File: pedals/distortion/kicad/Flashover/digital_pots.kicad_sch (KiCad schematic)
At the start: 5 parts, among them U7 MCP45HV51-104, U8 MCP45HV51-103, U9 MCP45HV51-103

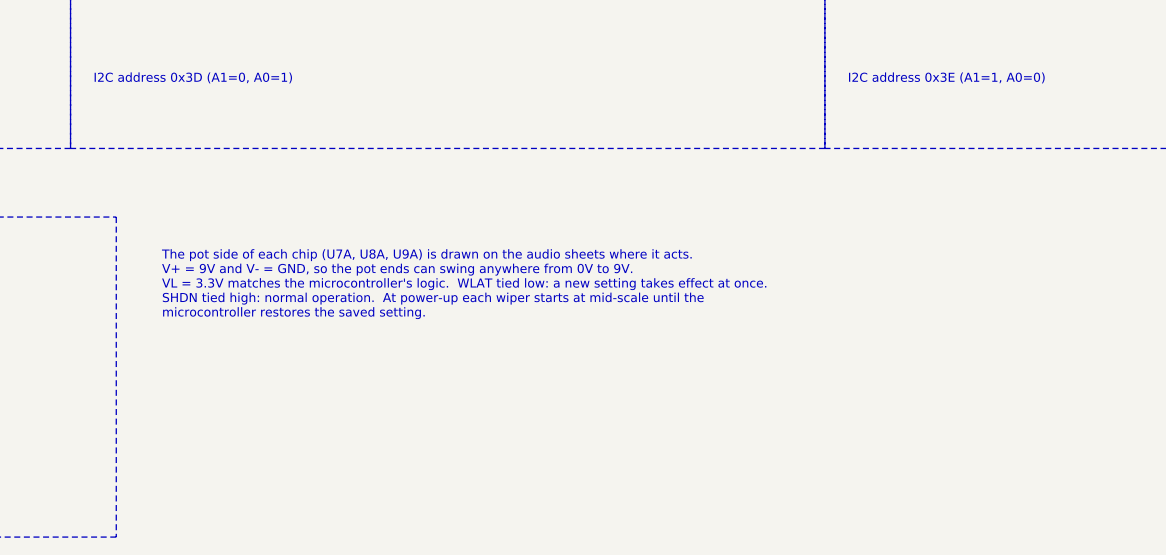
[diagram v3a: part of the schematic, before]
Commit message: Apply datasheet checks to Flashover
R33 = 15k (about 5 mA per LED, from the IS31FL3236A current formula).
R39 marked 33 ohm 0.5W per MIDI CA-033. R4 390 -> 330 because the
MCP45HV51 wiper resistance is about 150 ohms at 9V (below its 10V
specified range); sim model Rw updated to match. Pot symbol description
corrected to 8-bit. Product document records the check results.

Co-Authored-By: Claude Opus 5.5 <noreply@anthropic.com>
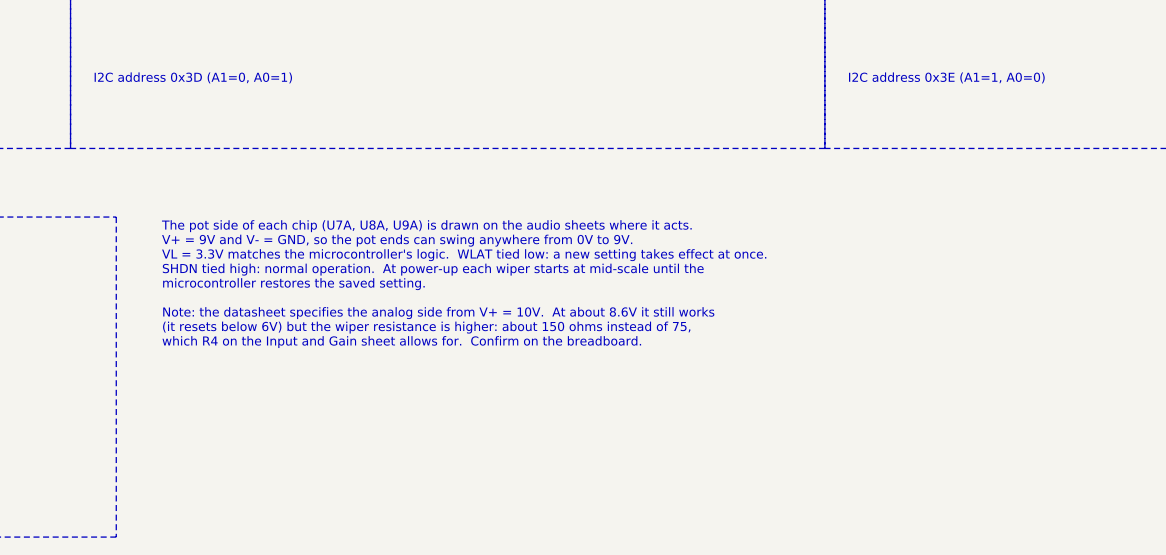
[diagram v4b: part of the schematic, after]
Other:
- note added: "The pot side of each chip (U7A, U8A, U9A) is drawn on the audio sheets where it acts. V+ = 9V and V- = GND, so the pot ends can swing anywhere from 0V to 9V. VL = 3.3V matches the microcontroller's logic. WLAT tied low: a new setting takes effect at once. SHDN tied high: normal operation. At power-up each wiper starts at mid-scale until the microcontroller restores the saved setting. Note: the da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"
- note removed: "The pot side of each chip (U7A, U8A, U9A) is drawn on the audio sheets where it acts. V+ = 9V and V- = GND, so the pot ends can swing anywhere from 0V to 9V. VL = 3.3V matches the microcontroller's logic. WLAT tied low: a new setting takes effect at once. SHDN tied high: normal operation. At power-up each wiper starts at mid-scale until the microcontroller restores the saved setting."
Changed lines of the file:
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@@
 		)
 	)
-	(text "The pot side of each chip (U7A, U8A, U9A) is drawn on the audio sheets where it acts.\nV+ = 9V and V- = GND, so the pot ends can swing anywhere from 0V to 9V.\nVL = 3.3V matches the microcontroller's logic.  WLAT tied low: a new setting takes effect at once.\nSHDN tied high: normal operation.  At power-up each wiper starts at mid-scale until the\nmicrocontroller restores the saved setting."
+	(text "The pot side of each chip (U7A, U8A, U9A) is drawn on the audio sheets where it acts.\nV+ = 9V and V- = GND, so the pot ends can swing anywhere from 0V to 9V.\nVL = 3.3V matches the microcontroller's logic.  WLAT tied low: a new setting takes effect at once.\nSHDN tied high: normal operation.  At power-up each wiper starts at mid-scale until the\nmicrocontroller restores the saved setting.\n\nNote: the datasheet specifies the analog side from V+ = 10V.  At about 8.6V it still works\n(it resets below 6V) but the wiper resistance is higher: about 150 ohms instead of 75,\nwhich R4 on the Input and Gain sheet allows for.  Confirm on the breadboard."
 		(exclude_from_sim no)
 		(at 114.3 144.78 0)
@@
 		(instances
 			(project "Flashover"
-				(path "/d44d1406-41c8-4e08-862e-64ff4a05b8dc/c09d2507-05e8-4731-b040-1c865b92845a"
+				(path "/d341370c-bf24-48b8-b9fb-db9600491445/a246cd81-fc52-4cad-ab94-507bb87b3303"
 					(reference "U7")
 					(unit 2)
@@
 		(instances
 			(project "Flashover"
-				(path "/d44d1406-41c8-4e08-862e-64ff4a05b8dc/c09d2507-05e8-4731-b040-1c865b92845a"
+				(path "/d341370c-bf24-48b8-b9fb-db9600491445/a246cd81-fc52-4cad-ab94-507bb87b3303"
 					(reference "#PWR57")
 					(unit 1)
@@
 		(instances
 			(project "Flashover"
-				(path "/d44d1406-41c8-4e08-862e-64ff4a05b8dc/c09d2507-05e8-4731-b040-1c865b92845a"
+				(path "/d341370c-bf24-48b8-b9fb-db9600491445/a246cd81-fc52-4cad-ab94-507bb87b3303"
 					(reference "#PWR58")
 					(unit 1)
@@
 		(instances
 			(project "Flashover"
-				(path "/d44d1406-41c8-4e08-862e-64ff4a05b8dc/c09d2507-05e8-4731-b040-1c865b92845a"
+				(path "/d341370c-bf24-48b8-b9fb-db9600491445/a246cd81-fc52-4cad-ab94-507bb87b3303"
 					(reference "#PWR59")
 					(unit 1)
@@
 		(instances
 			(project "Flashover"
-				(path "/d44d1406-41c8-4e08-862e-64ff4a05b8dc/c09d2507-05e8-4731-b040-1c865b92845a"
+				(path "/d341370c-bf24-48b8-b9fb-db9600491445/a246cd81-fc52-4cad-ab94-507bb87b3303"
 					(reference "#PWR60")
 					(unit 1)
@@
 		(instances
 			(project "Flashover"
-				(path "/d44d1406-41c8-4e08-862e-64ff4a05b8dc/c09d2507-05e8-4731-b040-1c865b92845a"
+				(path "/d341370c-bf24-48b8-b9fb-db9600491445/a246cd81-fc52-4cad-ab94-507bb87b3303"
 					(reference "#PWR61")
 					(unit 1)
@@
 		(instances
 			(project "Flashover"
-				(path "/d44d1406-41c8-4e08-862e-64ff4a05b8dc/c09d2507-05e8-4731-b040-1c865b92845a"
+				(path "/d341370c-bf24-48b8-b9fb-db9600491445/a246cd81-fc52-4cad-ab94-507bb87b3303"
 					(reference "#PWR62")
 					(unit 1)
@@
 		(instances
 			(project "Flashover"
-				(path "/d44d1406-41c8-4e08-862e-64ff4a05b8dc/c09d2507-05e8-4731-b040-1c865b92845a"
+				(path "/d341370c-bf24-48b8-b9fb-db9600491445/a246cd81-fc52-4cad-ab94-507bb87b3303"
 					(reference "#PWR63")
 					(unit 1)
@@
 		(instances
 			(project "Flashover"
-				(path "/d44d1406-41c8-4e08-862e-64ff4a05b8dc/c09d2507-05e8-4731-b040-1c865b92845a"
+				(path "/d341370c-bf24-48b8-b9fb-db9600491445/a246cd81-fc52-4cad-ab94-507bb87b3303"
 					(reference "U8")
 					(unit 2)
@@
 		(instances
 			(project "Flashover"
-				(path "/d44d1406-41c8-4e08-862e-64ff4a05b8dc/c09d2507-05e8-4731-b040-1c865b92845a"
+				(path "/d341370c-bf24-48b8-b9fb-db9600491445/a246cd81-fc52-4cad-ab94-507bb87b3303"
 					(reference "#PWR64")
 					(unit 1)
@@
 		(instances
 			(project "Flashover"
-				(path "/d44d1406-41c8-4e08-862e-64ff4a05b8dc/c09d2507-05e8-4731-b040-1c865b92845a"
+				(path "/d341370c-bf24-48b8-b9fb-db9600491445/a246cd81-fc52-4cad-ab94-507bb87b3303"
 					(reference "#PWR65")
 					(unit 1)
@@
 		(instances
 			(project "Flashover"
-				(path "/d44d1406-41c8-4e08-862e-64ff4a05b8dc/c09d2507-05e8-4731-b040-1c865b92845a"
+				(path "/d341370c-bf24-48b8-b9fb-db9600491445/a246cd81-fc52-4cad-ab94-507bb87b3303"
 					(reference "#PWR66")
 					(unit 1)
@@
 		(instances
 			(project "Flashover"
-				(path "/d44d1406-41c8-4e08-862e-64ff4a05b8dc/c09d2507-05e8-4731-b040-1c865b92845a"
+				(path "/d341370c-bf24-48b8-b9fb-db9600491445/a246cd81-fc52-4cad-ab94-507bb87b3303"
 					(reference "#PWR67")
 					(unit 1)
@@
 		(instances
 			(project "Flashover"
-				(path "/d44d1406-41c8-4e08-862e-64ff4a05b8dc/c09d2507-05e8-4731-b040-1c865b92845a"
+				(path "/d341370c-bf24-48b8-b9fb-db9600491445/a246cd81-fc52-4cad-ab94-507bb87b3303"
 					(reference "#PWR68")
 					(unit 1)
@@
 		(instances
 			(project "Flashover"
-				(path "/d44d1406-41c8-4e08-862e-64ff4a05b8dc/c09d2507-05e8-4731-b040-1c865b92845a"
+				(path "/d341370c-bf24-48b8-b9fb-db9600491445/a246cd81-fc52-4cad-ab94-507bb87b3303"
 					(reference "#PWR69")
 					(unit 1)
@@
 		(instances
 			(project "Flashover"
-				(path "/d44d1406-41c8-4e08-862e-64ff4a05b8dc/c09d2507-05e8-4731-b040-1c865b92845a"
+				(path "/d341370c-bf24-48b8-b9fb-db9600491445/a246cd81-fc52-4cad-ab94-507bb87b3303"
 					(reference "#PWR70")
 					(unit 1)
@@
 		(instances
 			(project "Flashover"
-				(path "/d44d1406-41c8-4e08-862e-64ff4a05b8dc/c09d2507-05e8-4731-b040-1c865b92845a"
+				(path "/d341370c-bf24-48b8-b9fb-db9600491445/a246cd81-fc52-4cad-ab94-507bb87b3303"
 					(reference "U9")
 					(unit 2)
@@
 		(instances
 			(project "Flashover"
-				(path "/d44d1406-41c8-4e08-862e-64ff4a05b8dc/c09d2507-05e8-4731-b040-1c865b92845a"
+				(path "/d341370c-bf24-48b8-b9fb-db9600491445/a246cd81-fc52-4cad-ab94-507bb87b3303"
 					(reference "#PWR71")
 					(unit 1)
@@
 		(instances
 			(project "Flashover"
-				(path "/d44d1406-41c8-4e08-862e-64ff4a05b8dc/c09d2507-05e8-4731-b040-1c865b92845a"
+				(path "/d341370c-bf24-48b8-b9fb-db9600491445/a246cd81-fc52-4cad-ab94-507bb87b3303"
 					(reference "#PWR72")
 					(unit 1)
@@
 		(instances
 			(project "Flashover"
-				(path "/d44d1406-41c8-4e08-862e-64ff4a05b8dc/c09d2507-05e8-4731-b040-1c865b92845a"
+				(path "/d341370c-bf24-48b8-b9fb-db9600491445/a246cd81-fc52-4cad-ab94-507bb87b3303"
 					(reference "#PWR73")
 					(unit 1)
@@
 		(instances
 			(project "Flashover"
-				(path "/d44d1406-41c8-4e08-862e-64ff4a05b8dc/c09d2507-05e8-4731-b040-1c865b92845a"
+				(path "/d341370c-bf24-48b8-b9fb-db9600491445/a246cd81-fc52-4cad-ab94-507bb87b3303"
 					(reference "#PWR74")
 					(unit 1)
@@
 		(instances
 			(project "Flashover"
-				(path "/d44d1406-41c8-4e08-862e-64ff4a05b8dc/c09d2507-05e8-4731-b040-1c865b92845a"
+				(path "/d341370c-bf24-48b8-b9fb-db9600491445/a246cd81-fc52-4cad-ab94-507bb87b3303"
 					(reference "#PWR75")
 					(unit 1)
@@
 		(instances
 			(project "Flashover"
-				(path "/d44d1406-41c8-4e08-862e-64ff4a05b8dc/c09d2507-05e8-4731-b040-1c865b92845a"
+				(path "/d341370c-bf24-48b8-b9fb-db9600491445/a246cd81-fc52-4cad-ab94-507bb87b3303"
 					(reference "#PWR76")
 					(unit 1)
@@
 		(instances
 			(project "Flashover"
-				(path "/d44d1406-41c8-4e08-862e-64ff4a05b8dc/c09d2507-05e8-4731-b040-1c865b92845a"
+				(path "/d341370c-bf24-48b8-b9fb-db9600491445/a246cd81-fc52-4cad-ab94-507bb87b3303"
 					(reference "#PWR77")
 					(unit 1)
@@
 		(instances
 			(project "Flashover"
-				(path "/d44d1406-41c8-4e08-862e-64ff4a05b8dc/c09d2507-05e8-4731-b040-1c865b92845a"
+				(path "/d341370c-bf24-48b8-b9fb-db9600491445/a246cd81-fc52-4cad-ab94-507bb87b3303"
 					(reference "R21")
 					(unit 1)
@@
 		(instances
 			(project "Flashover"
-				(path "/d44d1406-41c8-4e08-862e-64ff4a05b8dc/c09d2507-05e8-4731-b040-1c865b92845a"
+				(path "/d341370c-bf24-48b8-b9fb-db9600491445/a246cd81-fc52-4cad-ab94-507bb87b3303"
 					(reference "#PWR78")
 					(unit 1)
@@
 		(instances
 			(project "Flashover"
-				(path "/d44d1406-41c8-4e08-862e-64ff4a05b8dc/c09d2507-05e8-4731-b040-1c865b92845a"
+				(path "/d341370c-bf24-48b8-b9fb-db9600491445/a246cd81-fc52-4cad-ab94-507bb87b3303"
 					(reference "R22")
 					(unit 1)
@@
 		(instances
 			(project "Flashover"
-				(path "/d44d1406-41c8-4e08-862e-64ff4a05b8dc/c09d2507-05e8-4731-b040-1c865b92845a"
+				(path "/d341370c-bf24-48b8-b9fb-db9600491445/a246cd81-fc52-4cad-ab94-507bb87b3303"
 					(reference "#PWR79")
 					(unit 1)

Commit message: Assign Flashover footprints
Surface-mount for assembly; through-hole for jacks, encoders, panel LEDs,
the Soft/Hard button, the TO-220 regulator and the germanium diodes.
Q1/Q2 use the MMBT3904 symbol, 1N4148 -> 1N4148W, 1N5817 -> SS14.

Co-Authored-By: Claude Opus 5.5 <noreply@anthropic.com>
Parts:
- R21, R22: footprint (none) -> Resistor_SMD:R_0805_2012Metric
- U7, U8, U9: footprint (none) -> Package_SO:TSSOP-14_4.4x5mm_P0.65mm
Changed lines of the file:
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@@
 			(effects (font (size 1.27 1.27)))
 		)
-		(property "Footprint" ""
+		(property "Footprint" "Package_SO:TSSOP-14_4.4x5mm_P0.65mm"
 			(at 73.66 88.9 0)
 			(hide yes)
@@
 		(instances
 			(project "Flashover"
-				(path "/d341370c-bf24-48b8-b9fb-db9600491445/a246cd81-fc52-4cad-ab94-507bb87b3303"
+				(path "/872055d3-e01a-4a82-8c05-28c93674a700/288f9b5d-0dce-405c-aa6f-2a3071249c9f"
 					(reference "U7")
 					(unit 2)
@@
 		(instances
 			(project "Flashover"
-				(path "/d341370c-bf24-48b8-b9fb-db9600491445/a246cd81-fc52-4cad-ab94-507bb87b3303"
+				(path "/872055d3-e01a-4a82-8c05-28c93674a700/288f9b5d-0dce-405c-aa6f-2a3071249c9f"
 					(reference "#PWR57")
 					(unit 1)
@@
 		(instances
 			(project "Flashover"
-				(path "/d341370c-bf24-48b8-b9fb-db9600491445/a246cd81-fc52-4cad-ab94-507bb87b3303"
+				(path "/872055d3-e01a-4a82-8c05-28c93674a700/288f9b5d-0dce-405c-aa6f-2a3071249c9f"
 					(reference "#PWR58")
 					(unit 1)
@@
 		(instances
 			(project "Flashover"
-				(path "/d341370c-bf24-48b8-b9fb-db9600491445/a246cd81-fc52-4cad-ab94-507bb87b3303"
+				(path "/872055d3-e01a-4a82-8c05-28c93674a700/288f9b5d-0dce-405c-aa6f-2a3071249c9f"
 					(reference "#PWR59")
 					(unit 1)
@@
 		(instances
 			(project "Flashover"
-				(path "/d341370c-bf24-48b8-b9fb-db9600491445/a246cd81-fc52-4cad-ab94-507bb87b3303"
+				(path "/872055d3-e01a-4a82-8c05-28c93674a700/288f9b5d-0dce-405c-aa6f-2a3071249c9f"
 					(reference "#PWR60")
 					(unit 1)
@@
 		(instances
 			(project "Flashover"
-				(path "/d341370c-bf24-48b8-b9fb-db9600491445/a246cd81-fc52-4cad-ab94-507bb87b3303"
+				(path "/872055d3-e01a-4a82-8c05-28c93674a700/288f9b5d-0dce-405c-aa6f-2a3071249c9f"
 					(reference "#PWR61")
 					(unit 1)
@@
 		(instances
 			(project "Flashover"
-				(path "/d341370c-bf24-48b8-b9fb-db9600491445/a246cd81-fc52-4cad-ab94-507bb87b3303"
+				(path "/872055d3-e01a-4a82-8c05-28c93674a700/288f9b5d-0dce-405c-aa6f-2a3071249c9f"
 					(reference "#PWR62")
 					(unit 1)
@@
 		(instances
 			(project "Flashover"
-				(path "/d341370c-bf24-48b8-b9fb-db9600491445/a246cd81-fc52-4cad-ab94-507bb87b3303"
+				(path "/872055d3-e01a-4a82-8c05-28c93674a700/288f9b5d-0dce-405c-aa6f-2a3071249c9f"
 					(reference "#PWR63")
 					(unit 1)
@@
 			(effects (font (size 1.27 1.27)))
 		)
-		(property "Footprint" ""
+		(property "Footprint" "Package_SO:TSSOP-14_4.4x5mm_P0.65mm"
 			(at 157.48 88.9 0)
 			(hide yes)
@@
 		(instances
 			(project "Flashover"
-				(path "/d341370c-bf24-48b8-b9fb-db9600491445/a246cd81-fc52-4cad-ab94-507bb87b3303"
+				(path "/872055d3-e01a-4a82-8c05-28c93674a700/288f9b5d-0dce-405c-aa6f-2a3071249c9f"
 					(reference "U8")
 					(unit 2)
@@
 		(instances
 			(project "Flashover"
-				(path "/d341370c-bf24-48b8-b9fb-db9600491445/a246cd81-fc52-4cad-ab94-507bb87b3303"
+				(path "/872055d3-e01a-4a82-8c05-28c93674a700/288f9b5d-0dce-405c-aa6f-2a3071249c9f"
 					(reference "#PWR64")
 					(unit 1)
@@
 		(instances
 			(project "Flashover"
-				(path "/d341370c-bf24-48b8-b9fb-db9600491445/a246cd81-fc52-4cad-ab94-507bb87b3303"
+				(path "/872055d3-e01a-4a82-8c05-28c93674a700/288f9b5d-0dce-405c-aa6f-2a3071249c9f"
 					(reference "#PWR65")
 					(unit 1)
@@
 		(instances
 			(project "Flashover"
-				(path "/d341370c-bf24-48b8-b9fb-db9600491445/a246cd81-fc52-4cad-ab94-507bb87b3303"
+				(path "/872055d3-e01a-4a82-8c05-28c93674a700/288f9b5d-0dce-405c-aa6f-2a3071249c9f"
 					(reference "#PWR66")
 					(unit 1)
@@
 		(instances
 			(project "Flashover"
-				(path "/d341370c-bf24-48b8-b9fb-db9600491445/a246cd81-fc52-4cad-ab94-507bb87b3303"
+				(path "/872055d3-e01a-4a82-8c05-28c93674a700/288f9b5d-0dce-405c-aa6f-2a3071249c9f"
 					(reference "#PWR67")
 					(unit 1)
@@
 		(instances
 			(project "Flashover"
-				(path "/d341370c-bf24-48b8-b9fb-db9600491445/a246cd81-fc52-4cad-ab94-507bb87b3303"
+				(path "/872055d3-e01a-4a82-8c05-28c93674a700/288f9b5d-0dce-405c-aa6f-2a3071249c9f"
 					(reference "#PWR68")
 					(unit 1)
@@
 		(instances
 			(project "Flashover"
-				(path "/d341370c-bf24-48b8-b9fb-db9600491445/a246cd81-fc52-4cad-ab94-507bb87b3303"
+				(path "/872055d3-e01a-4a82-8c05-28c93674a700/288f9b5d-0dce-405c-aa6f-2a3071249c9f"
 					(reference "#PWR69")
 					(unit 1)
@@
 		(instances
 			(project "Flashover"
-				(path "/d341370c-bf24-48b8-b9fb-db9600491445/a246cd81-fc52-4cad-ab94-507bb87b3303"
+				(path "/872055d3-e01a-4a82-8c05-28c93674a700/288f9b5d-0dce-405c-aa6f-2a3071249c9f"
 					(reference "#PWR70")
 					(unit 1)
@@
 			(effects (font (size 1.27 1.27)))
 		)
-		(property "Footprint" ""
+		(property "Footprint" "Package_SO:TSSOP-14_4.4x5mm_P0.65mm"
 			(at 241.3 88.9 0)
 			(hide yes)
@@
 		(instances
 			(project "Flashover"
-				(path "/d341370c-bf24-48b8-b9fb-db9600491445/a246cd81-fc52-4cad-ab94-507bb87b3303"
+				(path "/872055d3-e01a-4a82-8c05-28c93674a700/288f9b5d-0dce-405c-aa6f-2a3071249c9f"
 					(reference "U9")
 					(unit 2)
@@
 		(instances
 			(project "Flashover"
-				(path "/d341370c-bf24-48b8-b9fb-db9600491445/a246cd81-fc52-4cad-ab94-507bb87b3303"
+				(path "/872055d3-e01a-4a82-8c05-28c93674a700/288f9b5d-0dce-405c-aa6f-2a3071249c9f"
 					(reference "#PWR71")
 					(unit 1)
@@
 		(instances
 			(project "Flashover"
-				(path "/d341370c-bf24-48b8-b9fb-db9600491445/a246cd81-fc52-4cad-ab94-507bb87b3303"
+				(path "/872055d3-e01a-4a82-8c05-28c93674a700/288f9b5d-0dce-405c-aa6f-2a3071249c9f"
 					(reference "#PWR72")
 					(unit 1)
@@
 		(instances
 			(project "Flashover"
-				(path "/d341370c-bf24-48b8-b9fb-db9600491445/a246cd81-fc52-4cad-ab94-507bb87b3303"
+				(path "/872055d3-e01a-4a82-8c05-28c93674a700/288f9b5d-0dce-405c-aa6f-2a3071249c9f"
 					(reference "#PWR73")
 					(unit 1)
@@
 		(instances
 			(project "Flashover"
-				(path "/d341370c-bf24-48b8-b9fb-db9600491445/a246cd81-fc52-4cad-ab94-507bb87b3303"
+				(path "/872055d3-e01a-4a82-8c05-28c93674a700/288f9b5d-0dce-405c-aa6f-2a3071249c9f"
 					(reference "#PWR74")
 					(unit 1)
@@
 		(instances
 			(project "Flashover"
-				(path "/d341370c-bf24-48b8-b9fb-db9600491445/a246cd81-fc52-4cad-ab94-507bb87b3303"
+				(path "/872055d3-e01a-4a82-8c05-28c93674a700/288f9b5d-0dce-405c-aa6f-2a3071249c9f"
 					(reference "#PWR75")
 					(unit 1)
@@
 		(instances
 			(project "Flashover"
-				(path "/d341370c-bf24-48b8-b9fb-db9600491445/a246cd81-fc52-4cad-ab94-507bb87b3303"
+				(path "/872055d3-e01a-4a82-8c05-28c93674a700/288f9b5d-0dce-405c-aa6f-2a3071249c9f"
 					(reference "#PWR76")
 					(unit 1)
@@
 		(instances
 			(project "Flashover"
-				(path "/d341370c-bf24-48b8-b9fb-db9600491445/a246cd81-fc52-4cad-ab94-507bb87b3303"
+				(path "/872055d3-e01a-4a82-8c05-28c93674a700/288f9b5d-0dce-405c-aa6f-2a3071249c9f"
 					(reference "#PWR77")
 					(unit 1)
@@
 			(effects (font (size 1.27 1.27)) (justify left))
 		)
-		(property "Footprint" ""
+		(property "Footprint" "Resistor_SMD:R_0805_2012Metric"
 			(at 35.56 149.86 0)
 			(hide yes)
@@
 		(instances
 			(project "Flashover"
-				(path "/d341370c-bf24-48b8-b9fb-db9600491445/a246cd81-fc52-4cad-ab94-507bb87b3303"
+				(path "/872055d3-e01a-4a82-8c05-28c93674a700/288f9b5d-0dce-405c-aa6f-2a3071249c9f"
 					(reference "R21")
 					(unit 1)
@@
 		(instances
 			(project "Flashover"
-				(path "/d341370c-bf24-48b8-b9fb-db9600491445/a246cd81-fc52-4cad-ab94-507bb87b3303"
+				(path "/872055d3-e01a-4a82-8c05-28c93674a700/288f9b5d-0dce-405c-aa6f-2a3071249c9f"
 					(reference "#PWR78")
 					(unit 1)
@@
 			(effects (font (size 1.27 1.27)) (justify left))
 		)
-		(property "Footprint" ""
+		(property "Footprint" "Resistor_SMD:R_0805_2012Metric"
 			(at 48.26 149.86 0)
 			(hide yes)
@@
 		(instances
 			(project "Flashover"
-				(path "/d341370c-bf24-48b8-b9fb-db9600491445/a246cd81-fc52-4cad-ab94-507bb87b3303"
+				(path "/872055d3-e01a-4a82-8c05-28c93674a700/288f9b5d-0dce-405c-aa6f-2a3071249c9f"
 					(reference "R22")
 					(unit 1)
@@
 		(instances
 			(project "Flashover"
-				(path "/d341370c-bf24-48b8-b9fb-db9600491445/a246cd81-fc52-4cad-ab94-507bb87b3303"
+				(path "/872055d3-e01a-4a82-8c05-28c93674a700/288f9b5d-0dce-405c-aa6f-2a3071249c9f"
 					(reference "#PWR79")
 					(unit 1)
